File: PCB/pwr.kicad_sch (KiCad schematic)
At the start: 21 parts, among them J1 Conn_01x02, J2 Conn_01x02, J3 Conn_01x04, J4 UJ2-MIBH2-4-SMT-TR, Q1 AO3401A, U1 LTC4412xS6, U2 TPS62172DSG, U3 USBLC6-2P6

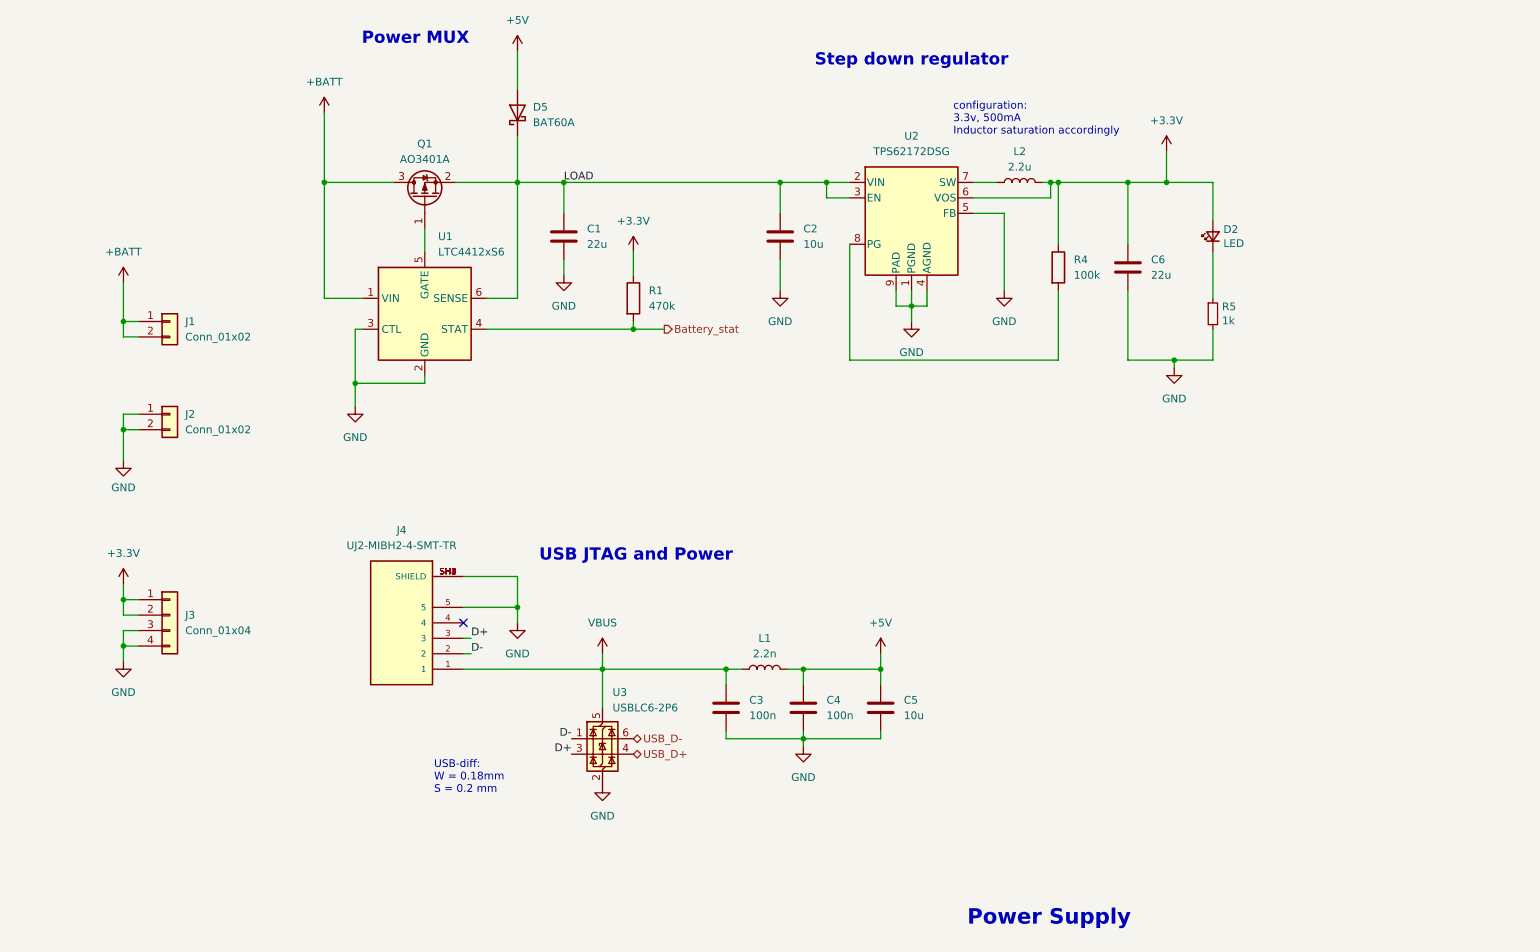
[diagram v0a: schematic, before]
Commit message: Added battery charging circuit and created WiFi api in firmware + created simple server for esp to send data to
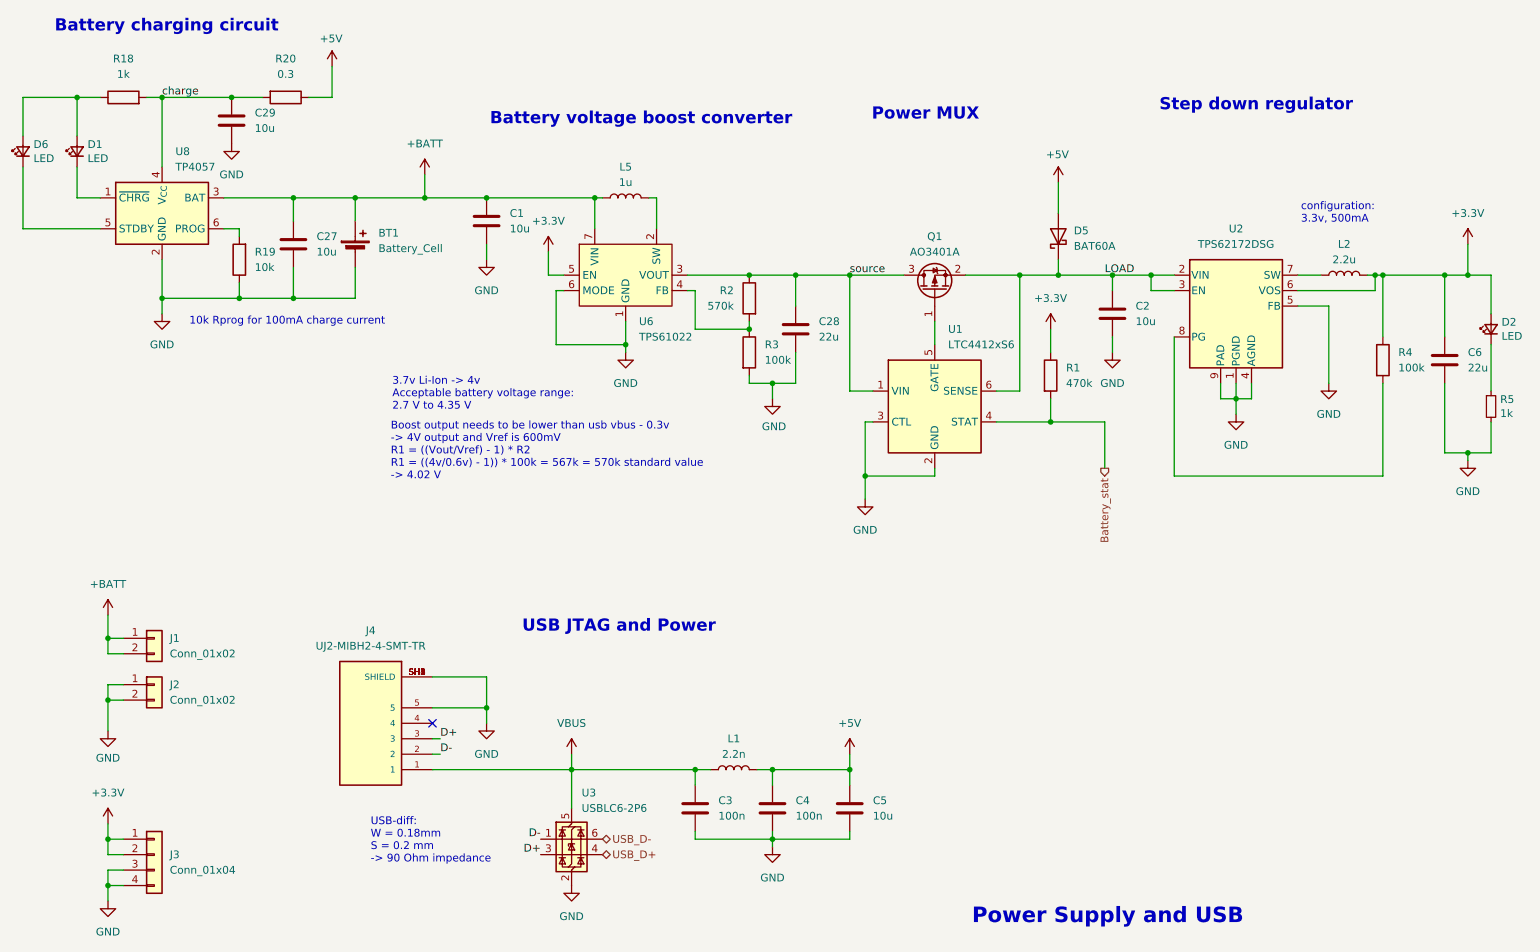
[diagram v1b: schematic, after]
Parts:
- added BT1: Battery_Cell, symbol Device:Battery_Cell
- added C27, C29: 10u, Capacitor_SMD:C_0603_1608Metric, symbol Device:C
- added C28: 22u, Capacitor_SMD:C_0805_2012Metric, symbol Device:C
- added D1, D6: LED, LED_SMD:LED_0805_2012Metric_Pad1.15x1.40mm_HandSolder, symbol Device:LED_Small
- added L5: 1u, Inductor_SMD:L_0805_2012Metric, symbol Device:L
- added R18: 1k, Resistor_SMD:R_0603_1608Metric, symbol Device:R
- added R19: 10k, Resistor_SMD:R_0402_1005Metric, symbol Device:R
- added R2: 570k, Resistor_SMD:R_0402_1005Metric, symbol Device:R
- added R20: 0.3, Resistor_SMD:R_0805_2012Metric, symbol Device:R
- added R3: 100k, Resistor_SMD:R_0402_1005Metric, symbol Device:R
- added U6: TPS61022, Package_DFN_QFN:Texas_RWU0007A_VQFN-7_2x2mm_P0.5mm, symbol Converter_DCDC:TPS61022
- added U8: TP4057, Package_TO_SOT_SMD:TSOT-23-6, symbol Battery_Management:TP4057
- C1: value 22u -> 10u; footprint Capacitor_SMD:C_0805_2012Metric -> Capacitor_SMD:C_0603_1608Metric
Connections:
- net +3.3V: now also U6.5 (EN)
- net +5V: now also R20.1
- net +BATT: now also C1.1, BT1.1 (+), C27.1, L5.1, U6.7 (VIN), U8.3 (BAT); no longer Q1.3 (D), U1.1 (VIN)
- net GND: now also BT1.2 (-), C27.2, C28.2, C29.2, R19.1, R3.2, U6.1 (GND), U6.6 (MODE), U8.2 (GND)
- net LOAD: no longer C1.1
- new net: L5.2, U6.2 (SW)
- new net: D1.2 (A), D6.2 (A), R18.1
- new net: D1.1 (K), U8.1 (~{CHRG})
- new net: D6.1 (K), U8.5 (STDBY)
- new net: R19.2, U8.6 (PROG)
- new net: R2.2, R3.1, U6.4 (FB)
- new net charge: C29.1, R18.2, R20.2, U8.4 (V_{CC})
- new net source: C28.1, Q1.3 (D), R2.1, U1.1 (VIN), U6.3 (VOUT)
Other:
- note added: "10k Rprog for 100mA charge current"
- note added: "3.7v Li-Ion -> 4v Acceptable battery voltage range: 2.7 V to 4.35 V"
- note added: "Battery charging circuit"
- note added: "Battery voltage boost converter"
- note added: "Boost output needs to be lower than usb vbus - 0.3v -> 4V output and Vref is 600mV R1 = ((Vout/Vref) - 1) * R2 R1 = ((4v/0.6v) - 1)) * 100k = 567k = 570k standard value -> 4.02 V"
- note added: "Power Supply and USB"
- note added: "USB-diff: W = 0.18mm S = 0.2 mm -> 90 Ohm impedance"
- note added: "configuration: 3.3v, 500mA"
- note removed: "Power Supply"
- note removed: "USB-diff: W = 0.18mm S = 0.2 mm"
- note removed: "configuration: 3.3v, 500mA Inductor saturation accordingly"
- moved on the sheet: C2, C3, C4, C5, C6, D2, D5, J1, J2, J3, J4, L1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

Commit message: Improvements and Neovim works correctly now
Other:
- note added: "10k Rprog for 100mA charge current Keep charcge current low, so that ESP can operate on usb power while battery is charging Imax_usb = 500mA"
- note removed: "10k Rprog for 100mA charge current"
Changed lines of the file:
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@@
 		)
 	)
-	(text "10k Rprog for 100mA charge current"
+	(text "10k Rprog for 100mA charge current\nKeep charcge current low, so that ESP can operate\non usb power while battery is charging \nImax_usb = 500mA"
 		(exclude_from_sim no)
-		(at 67.564 76.2 0)
+		(at 50.8 78.232 0)
 		(effects
 			(font
 				(size 1.27 1.27)
 			)
+			(justify left)
 		)
 	)
@@
 	(text "Boost output needs to be lower than usb vbus - 0.3v \n-> 4V output and Vref is 600mV\nR1 = ((Vout/Vref) - 1) * R2\nR1 = ((4v/0.6v) - 1)) * 100k = 567k = 570k standard value\n-> 4.02 V"
 		(exclude_from_sim no)
-		(at 84.582 97.536 0)
+		(at 95.758 102.362 0)
 		(effects
 			(font
@@
 	(text "3.7v Li-Ion -> 4v\nAcceptable battery voltage range:\n2.7 V to 4.35 V"
 		(exclude_from_sim no)
-		(at 84.836 88.138 0)
+		(at 96.012 92.964 0)
 		(effects
 			(font

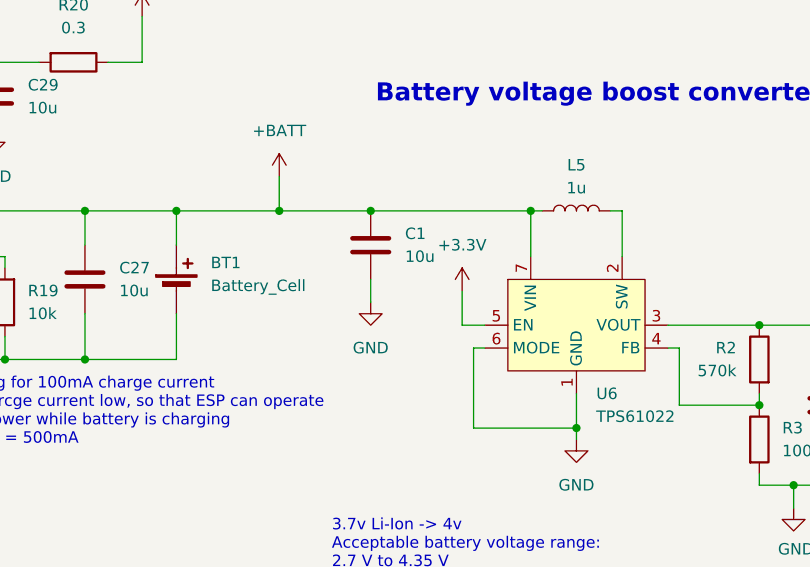
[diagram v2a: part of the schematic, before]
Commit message: Updated some component packages
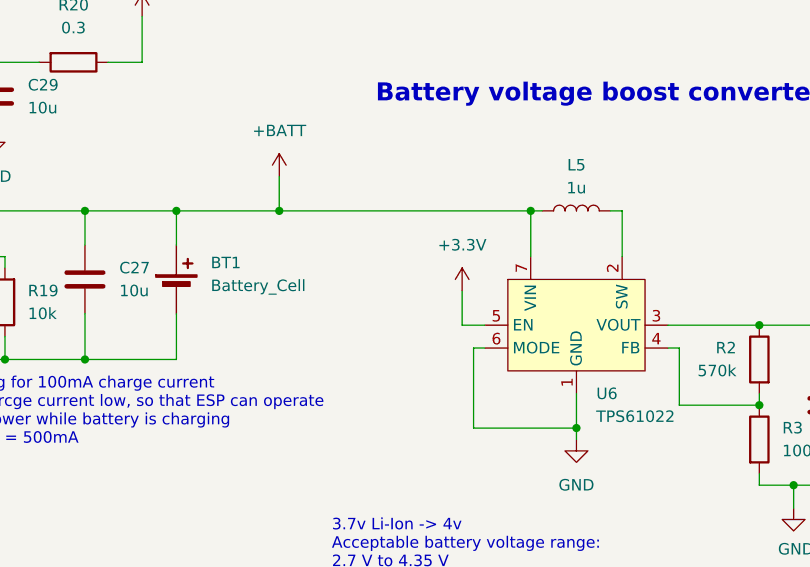
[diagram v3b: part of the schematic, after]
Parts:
- removed C1: 10u, Capacitor_SMD:C_0603_1608Metric, symbol Device:C
- L2: footprint Inductor_SMD:L_0805_2012Metric -> Inductor_SMD:L_1008_2520Metric
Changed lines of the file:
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@@
 	)
 	(junction
-		(at 100.33 55.88)
-		(diameter 0)
-		(color 0 0 0 0)
-	)
-	(junction
 		(at 223.52 88.9)
 		(diameter 0)
@@
 	(wire
 		(pts
-			(xy 90.17 55.88) (xy 100.33 55.88)
+			(xy 90.17 55.88) (xy 118.11 55.88)
 		)
 		(stroke
@@
 	(wire
 		(pts
-			(xy 100.33 63.5) (xy 100.33 66.04)
-		)
-		(stroke
-			(width 0)
-			(type default)
-		)
-	)
-	(wire
-		(pts
 			(xy 118.11 55.88) (xy 118.11 60.96)
 		)
@@
 	(wire
 		(pts
-			(xy 100.33 55.88) (xy 118.11 55.88)
-		)
-		(stroke
-			(width 0)
-			(type default)
-		)
-	)
-	(wire
-		(pts
 			(xy 203.2 68.58) (xy 209.55 68.58)
 		)
@@
 	(label "D-"
 		(at 92.71 147.32 0)
-		(fields_autoplaced yes)
 		(effects
 			(font
@@
 	(label "D+"
 		(at 92.71 144.78 0)
-		(fields_autoplaced yes)
 		(effects
 			(font
@@
 	(label "D+"
 		(at 109.22 163.83 180)
-		(fields_autoplaced yes)
 		(effects
 			(font
@@
 	(label "LOAD"
 		(at 201.93 68.58 0)
-		(fields_autoplaced yes)
 		(effects
 			(font
@@
 	(label "source"
 		(at 160.02 68.58 0)
-		(fields_autoplaced yes)
 		(effects
 			(font
@@
 	(label "D-"
 		(at 109.22 161.29 180)
-		(fields_autoplaced yes)
 		(effects
 			(font
@@
 	(label "charge"
 		(at 46.99 39.37 0)
-		(fields_autoplaced yes)
 		(effects
 			(font
@@
 		(shape output)
 		(at 201.93 100.33 270)
-		(fields_autoplaced yes)
 		(effects
 			(font
@@
 		(shape bidirectional)
 		(at 119.38 161.29 0)
-		(fields_autoplaced yes)
 		(effects
 			(font
@@
 		(shape bidirectional)
 		(at 119.38 163.83 0)
-		(fields_autoplaced yes)
 		(effects
 			(font
@@
 			)
 		)
-		(property "Footprint" "Inductor_SMD:L_0805_2012Metric"
+		(property "Footprint" "Inductor_SMD:L_1008_2520Metric"
 			(at 241.3 68.58 0)
 			(effects
@@
 	)
 	(symbol
-		(lib_id "Device:C")
-		(at 100.33 59.69 0)
-		(unit 1)
-		(exclude_from_sim no)
-		(in_bom yes)
-		(on_board yes)
-		(dnp no)
-		(fields_autoplaced yes)
-		(property "Reference" "C1"
-			(at 104.14 58.4199 0)
-			(effects
-				(font
-					(size 1.27 1.27)
-				)
-				(justify left)
-			)
-		)
-		(property "Value" "10u"
-			(at 104.14 60.9599 0)
-			(effects
-				(font
-					(size 1.27 1.27)
-				)
-				(justify left)
-			)
-		)
-		(property "Footprint" "Capacitor_SMD:C_0603_1608Metric"
-			(at 101.2952 63.5 0)
-			(effects
-				(font
-					(size 1.27 1.27)
-				)
-				(hide yes)
-			)
-		)
-		(property "Datasheet" "~"
-			(at 100.33 59.69 0)
-			(effects
-				(font
-					(size 1.27 1.27)
-				)
-				(hide yes)
-			)
-		)
-		(property "Description" "Unpolarized capacitor"
-			(at 100.33 59.69 0)
-			(effects
-				(font
-					(size 1.27 1.27)
-				)
-				(hide yes)
-			)
-		)
-		(pin "2"
-		)
-		(pin "1"
-		)
-		(instances
-			(project ""
-				(path "/357055bf-c309-4d6b-a2fa-f5ee5ba59771/98819006-dc75-4aad-a220-e6960b29e68b"
-					(reference "C1")
-					(unit 1)
-				)
-			)
-		)
-	)
-	(symbol
 		(lib_id "UJ2-MIBH2-4-SMT-TR:UJ2-MIBH2-4-SMT-TR")
 		(at 81.28 142.24 180)
@@
 					(unit 1)
 				)
-			)
-		)
-	)
-	(symbol
-		(lib_name "GND_2")
-		(lib_id "power:GND")
-		(at 100.33 66.04 0)
-		(unit 1)
-		(exclude_from_sim no)
-		(in_bom yes)
-		(on_board yes)
-		(dnp no)
-		(fields_autoplaced yes)
-		(property "Reference" "#PWR050"
-			(at 100.33 72.39 0)
-			(effects
-				(font
-					(size 1.27 1.27)
-				)
-				(hide yes)
-			)
-		)
-		(property "Value" "GND"
-			(at 100.33 71.12 0)
-			(effects
-				(font
-					(size 1.27 1.27)
-				)
-			)
-		)
-		(property "Footprint" ""
-			(at 100.33 66.04 0)
-			(effects
-				(font
-					(size 1.27 1.27)
-				)
-				(hide yes)
-			)
-		)
-		(property "Datasheet" ""
-			(at 100.33 66.04 0)
-			(effects
-				(font
-					(size 1.27 1.27)
-				)
-				(hide yes)
-			)
-		)
-		(property "Description" "Power symbol creates a global label with name \"GND\" , ground"
-			(at 100.33 66.04 0)
-			(effects
-				(font
-					(size 1.27 1.27)
-				)
-				(hide yes)
-			)
-		)
-		(pin "1"
-		)
-		(instances
-			(project "Plant-health-meter"
-				(path "/357055bf-c309-4d6b-a2fa-f5ee5ba59771/98819006-dc75-4aad-a220-e6960b29e68b"
-					(reference "#PWR050")
-					(unit 1)
-				)

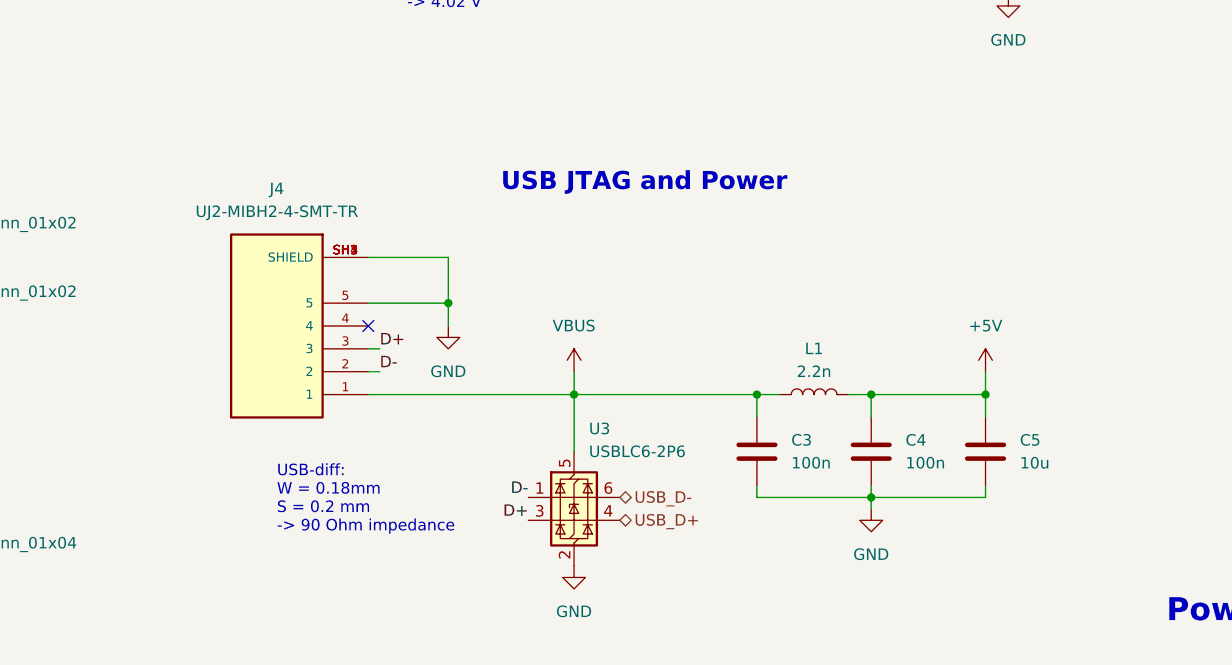
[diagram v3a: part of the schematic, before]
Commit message: removed usb port library
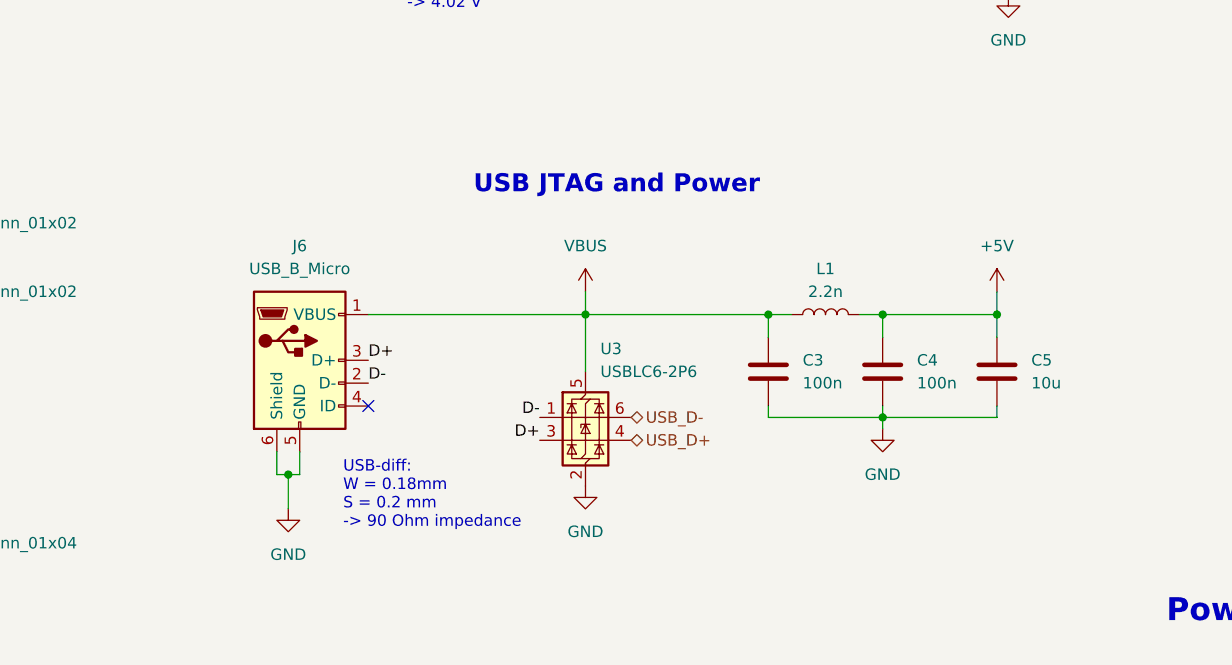
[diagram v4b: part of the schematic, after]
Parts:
- removed J4: UJ2-MIBH2-4-SMT-TR, UJ2-MIBH2-4-SMT-TR:CUI_UJ2-MIBH2-4-SMT-TR, symbol UJ2-MIBH2-4-SMT-TR:UJ2-MIBH2-4-SMT-TR
- added J6: USB_B_Micro, Connector_USB:USB_Micro-B_Molex-105017-0001, symbol Connector:USB_B_Micro
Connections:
- net D+: now also J6.3 (D+)
- net D-: now also J6.2 (D-)
- net GND: now also J6.5 (GND), J6.6 (Shield)
- net VBUS: now also J6.1 (VBUS)
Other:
- moved on the sheet: C3, C4, C5, L1, U3

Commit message: latest
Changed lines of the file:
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@@
 	(text "Power MUX"
 		(exclude_from_sim no)
-		(at 172.466 42.164 0)
+		(at 173.228 42.672 0)
 		(effects
 			(font
